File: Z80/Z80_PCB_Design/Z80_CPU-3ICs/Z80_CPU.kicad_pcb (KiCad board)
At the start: 2 copper layers, 95 x 95 mm, 47 parts, among them J1 USB_B, J2 Conn_01x12, J3 Conn_01x12, J4 Conn_01x02, U1 Z80CPU, U2 AS6C4008, U3 4.9152 MHz, U4 CY8C5267AXI-LP051, U5 MCP23017_SP, Y1 32.768KHz

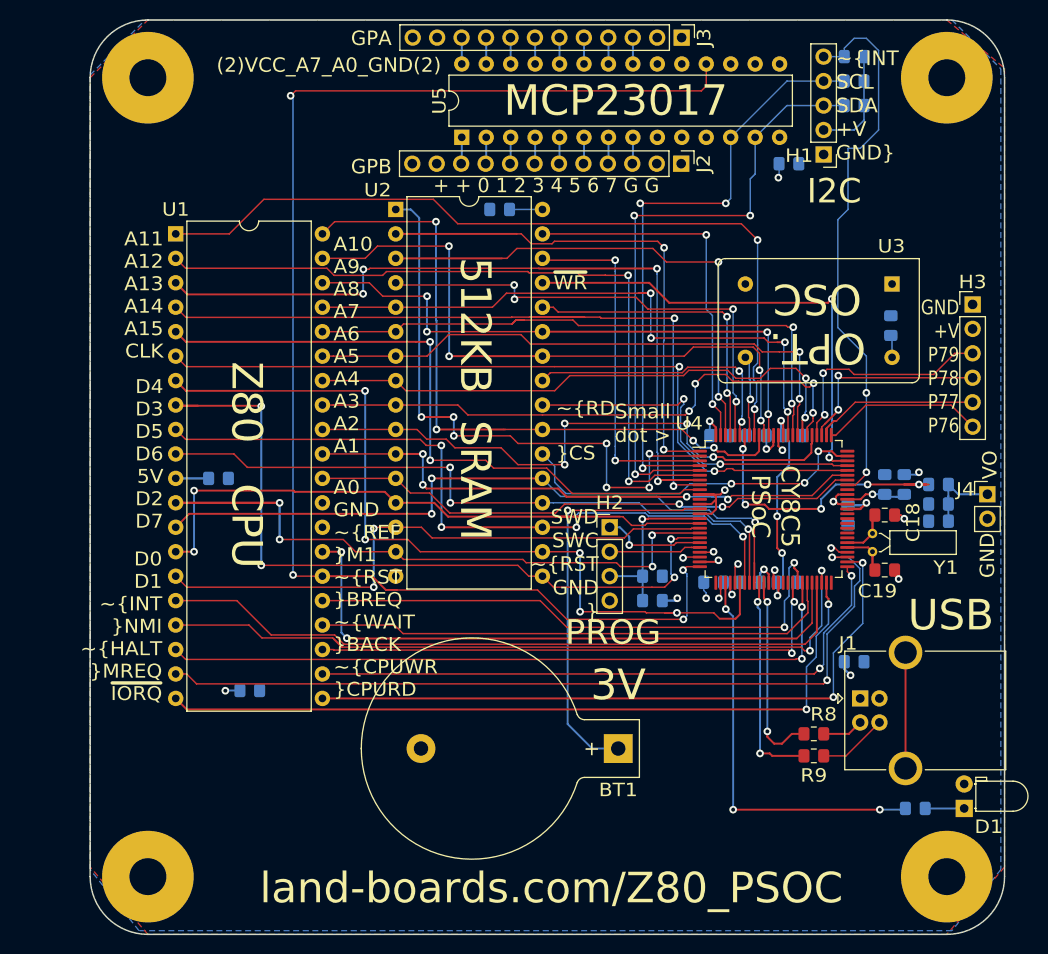
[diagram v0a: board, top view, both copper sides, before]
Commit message: Grand Piano on DAC8 output
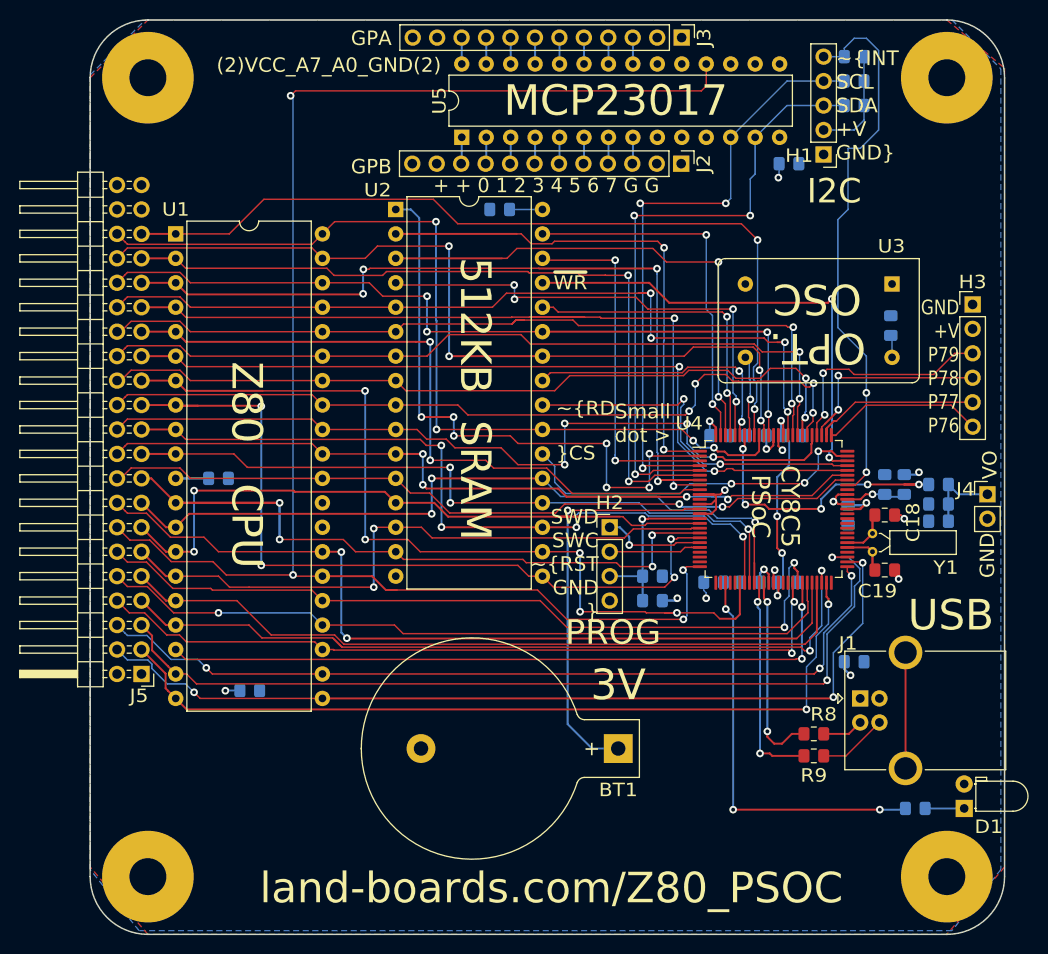
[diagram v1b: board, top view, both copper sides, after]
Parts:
- added J5: Conn_02x20_Odd_Even, Connector_PinHeader_2.54mm:PinHeader_2x21_P2.54mm_Horizontal, F.Cu at (5.33, 67.9)
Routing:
- net /~CPURD: track 70.0 -> 93.7 mm, vias 2 -> 3
- net /~WAIT: track 54.9 -> 78.3 mm, vias 0 -> 1
- net /~BUSRQ: track 58.5 -> 81.9 mm
- net /~M1: track 64.4 -> 87.8 mm
- net /~CPUWR: track 64.0 -> 87.5 mm, vias 2 -> 3
- net /~BUSACK: track 56.4 -> 79.9 mm
- net /CPUA8: track 61.3 -> 83.5 mm
- net /CPUA7: track 64.6 -> 86.9 mm
- net /CPUA6: track 62.6 -> 84.8 mm
- net /CPUA5: track 60.0 -> 82.2 mm
- net /CPUA4: track 58.8 -> 81.0 mm
- net /CPUA1: track 73.1 -> 95.4 mm
- net /CPUA0: track 57.7 -> 79.9 mm
- net /CPUA9: track 67.2 -> 89.4 mm
- net /CPUA3: track 60.9 -> 83.1 mm
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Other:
- board text added: "REV 3"
- board text removed: "A0 GND ~REF ~M1 ~RST ~BREQ ~WAIT ~BACK ~CPUWR ~CPURD"
- board text removed: "A10 A9 A8 A7 A6 A5 A4 A3 A2 A1"
- board text removed: "A11 A12 A13 A14 A15 CLK"
- board text removed: "D0 D1 ~INT ~NMI ~HALT ~MREQ ~IORQ"
- board text removed: "D4 D3 D5 D6 5V D2 D7"
- board text removed: "REV 2"

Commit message: pio init stuck z80
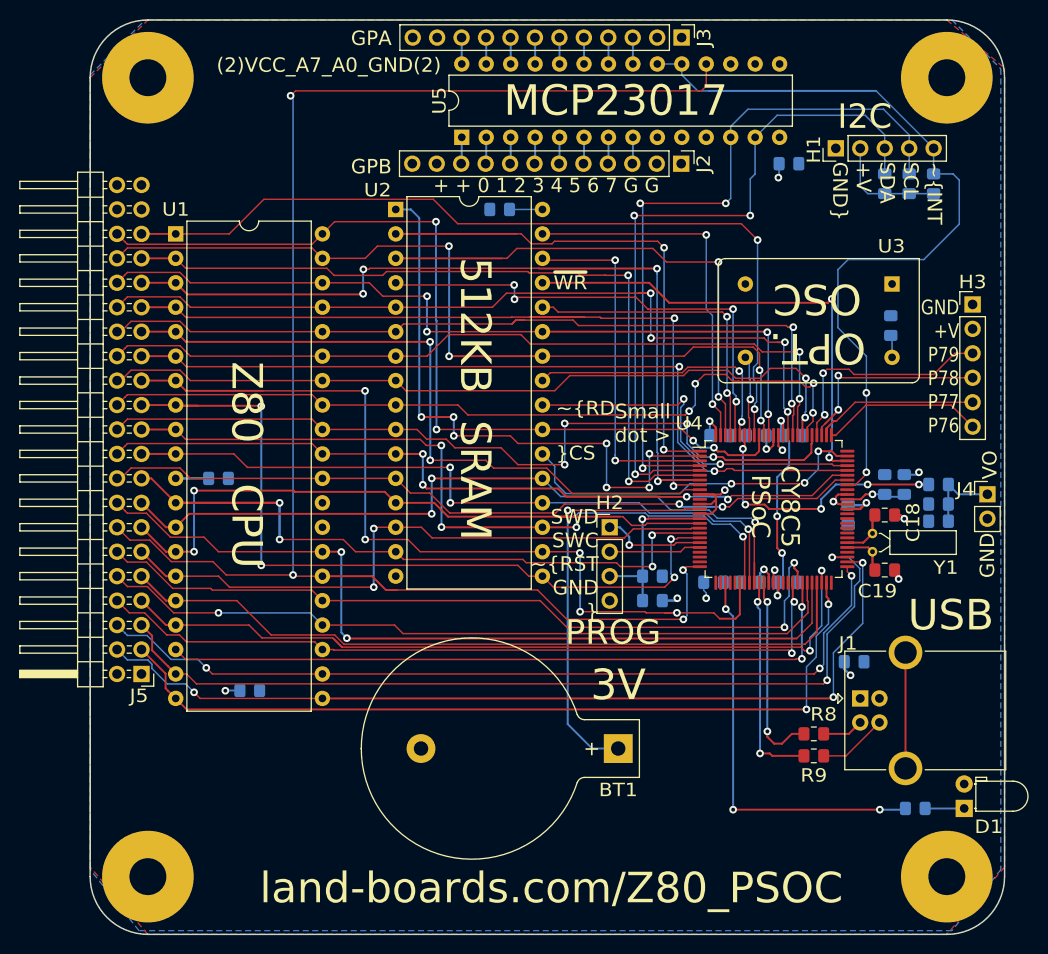
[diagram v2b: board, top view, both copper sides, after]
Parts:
- C18, C19: value 8pF -> 18pF
- R1: value 2.2K -> 10K
- moved R1 15.6 mm to (87.6, 17.0), turned to 90 degrees
- moved R2 12.1 mm to (85.1, 17.0), turned to 90 degrees
- moved R3 8.73 mm to (82.5, 17.0), turned to 90 degrees
- moved H1 1.42 mm to (77.5, 13.3), turned to 90 degrees
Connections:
- U5 pad 19: (no net) -> /~I2CINT
- U5 pad 20: (no net) -> /~I2CINT
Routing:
- net /~I2CINT: track 57.5 -> 100.0 mm
- net /SCL: track 63.9 -> 75.2 mm
- net /SDA: track 64.8 -> 73.5 mm
- net /DAC_OUT: track 29.8 -> 28.3 mm
- net +5V: track 39.8 -> 40.4 mm

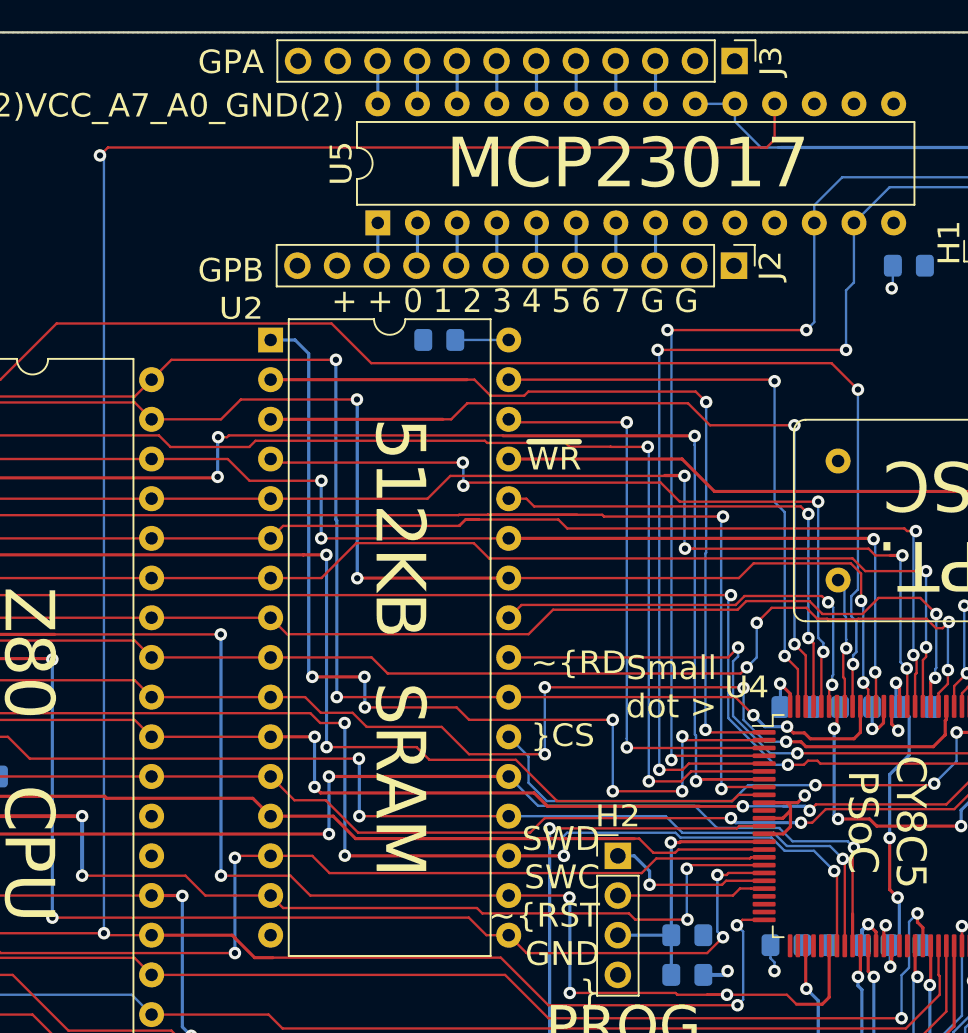
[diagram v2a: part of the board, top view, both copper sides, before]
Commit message: remove cpu reset from expansion mcp23017
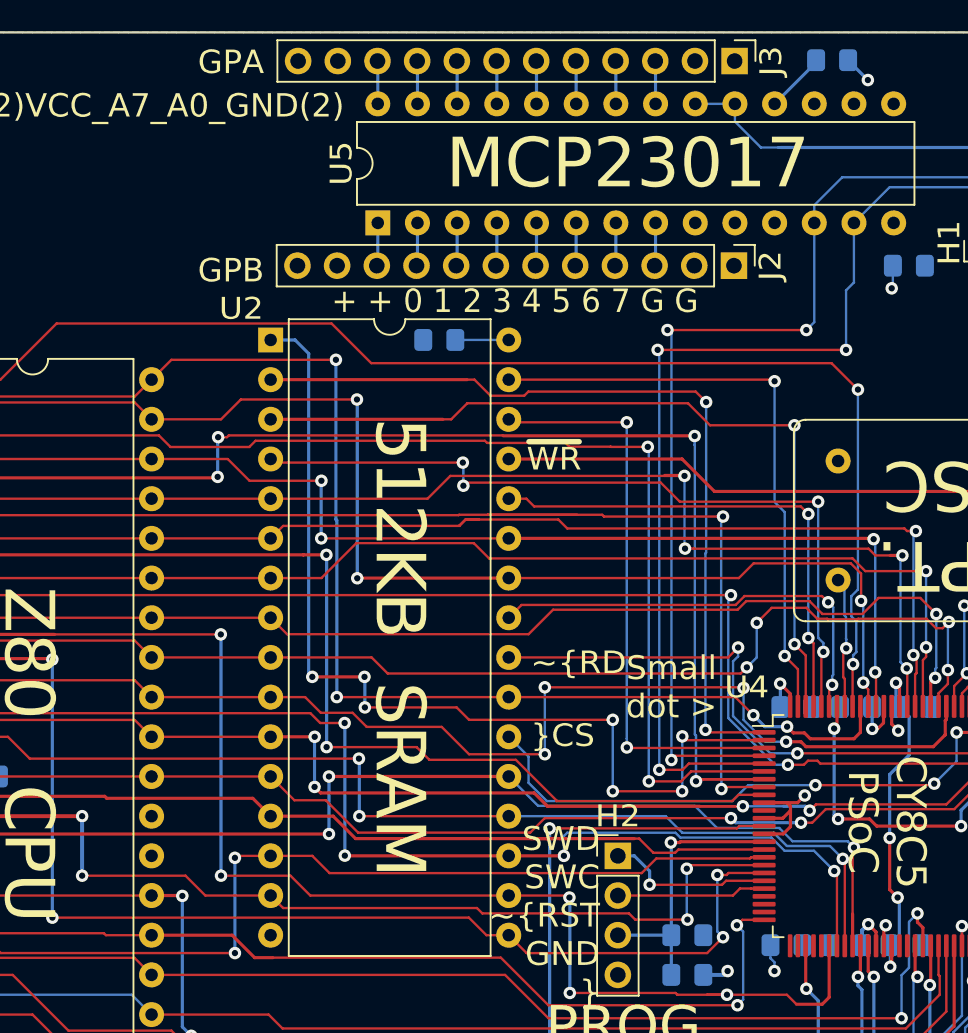
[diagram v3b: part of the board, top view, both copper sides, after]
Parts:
- added R10: 10K, Resistor_SMD:R_0805_2012Metric_Pad1.15x1.40mm_HandSolder, B.Cu at (67.7, 1.78)
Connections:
- U5 pad 18: /~CPURST -> Net-(R10-Pad2)
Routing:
- net /~CPURST: track 165.9 -> 70.1 mm, vias 4 -> 2
- net Net-(R10-Pad2): track 0.00 -> 3.89 mm
- net +5V: track 40.4 -> 42.2 mm, vias 9 -> 10
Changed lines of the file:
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@@
     (thickness 1.6)
     (drawings 33)
-    (tracks 1241)
+    (tracks 1238)
     (zones 0)
-    (modules 48)
-    (nets 93)
+    (modules 49)
+    (nets 94)
   )
   (page A)
@@
   )
   (setup
-    (last_trace_width 0.1524)
+    (last_trace_width 0.2032)
     (user_trace_width 0.1524)
     (trace_clearance 0.1524)
@@
   (net 91 "Net-(C18-Pad2)")
   (net 92 "Net-(C19-Pad2)")
+  (net 93 "Net-(R10-Pad2)")
   (net_class Default "This is the default net class."
     (clearance 0.1524)
@@
     (add_net "Net-(D1-Pad1)")
     (add_net "Net-(J1-Pad5)")
+    (add_net "Net-(R10-Pad2)")
     (add_net "Net-(R7-Pad2)")
     (add_net "Net-(R8-Pad2)")
@@
     (add_net "Net-(U3-Pad8)")
   )
+  (module Resistor_SMD:R_0805_2012Metric_Pad1.15x1.40mm_HandSolder (layer B.Cu)
+    (at 67.691 1.778 180)
+    (descr "Resistor SMD 0805 (2012 Metric), square (rectangular) end terminal, IPC_7351 nominal with elongated pad for handsoldering. (Body size source: https://docs.google.com/spreadsheets/d/1BsfQQcO9C6DZCsRaXUlFlo91Tg2WpOkGARC1WS5S8t0/edit?usp=sharing), generated with kicad-footprint-generator")
+    (tags "resistor handsolder")
+    (attr smd)
+    (fp_text reference R10 (at -4.318 0 180) (layer B.SilkS)
+      (effects (font (size 1.397 1.524) (thickness 0.254)) (justify mirror))
+    )
+    (fp_text value 10K (at 0 -1.65 180) (layer B.Fab)
+      (effects (font (size 1 1) (thickness 0.15)) (justify mirror))
+    )
+    (fp_line (start -1 -0.6) (end -1 0.6) (layer B.Fab) (width 0.1))
+    (fp_line (start -1 0.6) (end 1 0.6) (layer B.Fab) (width 0.1))
+    (fp_line (start 1 0.6) (end 1 -0.6) (layer B.Fab) (width 0.1))
+    (fp_line (start 1 -0.6) (end -1 -0.6) (layer B.Fab) (width 0.1))
+    (fp_line (start -0.261252 0.71) (end 0.261252 0.71) (layer B.SilkS) (width 0.12))
+    (fp_line (start -0.261252 -0.71) (end 0.261252 -0.71) (layer B.SilkS) (width 0.12))
+    (fp_line (start -1.85 -0.95) (end -1.85 0.95) (layer B.CrtYd) (width 0.05))
+    (fp_line (start -1.85 0.95) (end 1.85 0.95) (layer B.CrtYd) (width 0.05))
+    (fp_line (start 1.85 0.95) (end 1.85 -0.95) (layer B.CrtYd) (width 0.05))
+    (fp_line (start 1.85 -0.95) (end -1.85 -0.95) (layer B.CrtYd) (width 0.05))
+    (fp_text user %R (at 0 0 180) (layer B.Fab)
+      (effects (font (size 0.5 0.5) (thickness 0.08)) (justify mirror))
+    )
+    (pad 1 smd roundrect (at -1.025 0 180) (size 1.15 1.4) (layers B.Cu B.Paste B.Mask) (roundrect_rratio 0.217391)
+      (net 2 +5V))
+    (pad 2 smd roundrect (at 1.025 0 180) (size 1.15 1.4) (layers B.Cu B.Paste B.Mask) (roundrect_rratio 0.217391)
+      (net 93 "Net-(R10-Pad2)"))
+    (model ${KISYS3DMOD}/Resistor_SMD.3dshapes/R_0805_2012Metric.wrl
+      (at (xyz 0 0 0))
+      (scale (xyz 1 1 1))
+      (rotate (xyz 0 0 0))
+    )
+  )
   (module Inductor_SMD:L_0805_2012Metric_Pad1.15x1.40mm_HandSolder (layer B.Cu)
     (at 84.582 48.26 90)
@@
       (net 73 /GPB3))
     (pad 18 thru_hole oval (at 7.62 25.4 90) (size 1.6 1.6) (drill 0.8) (layers *.Cu *.Mask)
-      (net 21 /~CPURST))
+      (net 93 "Net-(R10-Pad2)"))
     (pad 5 thru_hole oval (at 0 10.16 90) (size 1.6 1.6) (drill 0.8) (layers *.Cu *.Mask)
       (net 74 /GPB4))
@@
     )
   )
+  (gr_text MCP23017 (at 54.61 8.382) (layer F.SilkS)
+    (effects (font (size 3.175 3.175) (thickness 0.79375)))
+  )
   (gr_text "~RD\n\n~CS" (at 48.387 42.672) (layer F.SilkS)
     (effects (font (size 1.4478 1.524) (thickness 0.34925)) (justify left))
@@
     (effects (font (size 1.5 1.5) (thickness 0.3)))
   )
-  (gr_text MCP23017 (at 54.61 8.382) (layer F.SilkS)
-    (effects (font (size 3.175 3.175) (thickness 0.79375)))
-  )
   (gr_text "GND\n+V\nP79\nP78\nP77\nP76" (at 90.297 36.0045) (layer F.SilkS)
     (effects (font (size 1.524 1.27) (thickness 0.3175)) (justify right))
@@
   (segment (start 82.55 18.043) (end 83.35 18.043) (width 0.1524) (layer B.Cu) (net 2))
   (segment (start 85.09 18.043) (end 87.63 18.043) (width 0.1524) (layer B.Cu) (net 2))
+  (via (at 69.977 3.048) (size 0.8) (drill 0.4) (layers F.Cu B.Cu) (net 2))
+  (segment (start 68.716 1.778) (end 68.716 1.787) (width 0.2032) (layer B.Cu) (net 2))
+  (segment (start 68.716 1.787) (end 69.977 3.048) (width 0.2032) (layer B.Cu) (net 2))
   (via (at 49.6062 50.946999) (size 0.8) (drill 0.4) (layers F.Cu B.Cu) (net 3))
   (segment (start 61.595 50.946999) (end 49.6062 50.946999) (width 0.1524) (layer F.Cu) (net 3))
@@
   (segment (start 31.890599 59.220999) (end 30.724921 59.220999) (width 0.2032) (layer F.Cu) (net 21))
   (segment (start 30.724921 59.220999) (end 29.288922 57.785) (width 0.2032) (layer F.Cu) (net 21))
-  (via (at 21.082 57.658) (size 0.8) (drill 0.4) (layers F.Cu B.Cu) (net 21))
   (segment (start 24.13 57.785) (end 21.209 57.785) (width 0.1524) (layer F.Cu) (net 21) (status 10))
   (segment (start 21.209 57.785) (end 21.082 57.658) (width 0.1524) (layer F.Cu) (net 21))
-  (via (at 20.828 7.874) (size 0.8) (drill 0.4) (layers F.Cu B.Cu) (net 21))
-  (segment (start 21.082 57.658) (end 21.082 8.128) (width 0.1524) (layer B.Cu) (net 21))
-  (segment (start 21.082 8.128) (end 20.828 7.874) (width 0.1524) (layer B.Cu) (net 21))
-  (segment (start 20.828 7.874) (end 21.336 7.366) (width 0.1524) (layer F.Cu) (net 21))
-  (segment (start 21.336 7.366) (end 63.5 7.366) (width 0.1524) (layer F.Cu) (net 21))
-  (segment (start 64.008 6.858) (end 64.008 4.572) (width 0.1524) (layer F.Cu) (net 21) (status 20))
-  (segment (start 63.5 7.366) (end 64.008 6.858) (width 0.1524) (layer F.Cu) (net 21))
   (via (at 61.595 57.15) (size 0.8) (drill 0.4) (layers F.Cu B.Cu) (net 21))
   (segment (start 63.3375 56.8) (end 61.945 56.8) (width 0.1524) (layer F.Cu) (net 21) (status 10))
@@
   (segment (start 80.835 54.8) (end 81.28 55.245) (width 0.2032) (layer F.Cu) (net 92) (status 20))
   (segment (start 78.6625 54.8) (end 80.835 54.8) (width 0.2032) (layer F.Cu) (net 92) (status 10))
+  (segment (start 66.666 1.914) (end 66.666 1.778) (width 0.2032) (layer B.Cu) (net 93))
+  (segment (start 64.008 4.572) (end 66.666 1.914) (width 0.2032) (layer B.Cu) (net 93))
   (zone (net 2) (net_name +5V) (layer F.Cu) (hatch edge 0.508)
     (connect_pads (clearance 0.2032))
